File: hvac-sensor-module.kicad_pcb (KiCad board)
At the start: 2 copper layers, 30 x 41 mm, 53 parts, among them J1 Conn_01x04, P1 Debug, Q1 RSS060P05FRATB, SW1 SW_PUSH, SW2 SW_PUSH, SW3 SW_PUSH, U1 LMR16006, U2 HDC1080, U3 STM32F072C8Tx, U5 TCAN334, X1 32.768KHz 12.5pF

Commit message: Layout finished.
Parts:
- removed C10, C12: 15p, Capacitor_SMD:C_0603_1608Metric_Pad1.05x0.95mm_HandSolder
- removed C2: 0.1F, villa-control:CP_Radial_D13.0mm_P10mm
- removed D3: 0.3V, villa-control:D_SOD-123_HandSolder
- removed R3: 100, Resistors_SMD:R_0603_HandSoldering
- removed the REF** at (124.0, 92.0)
- removed W2: 3.3V, TestPoint:TestPoint_THTPad_D1.5mm_Drill0.7mm
- removed W3: GND, TestPoint:TestPoint_THTPad_1.5x1.5mm_Drill0.7mm
- removed X1: 32.768KHz 12.5pF, villa-control:Crystal-MS1V-T1K
- added C18: 4µ7, Capacitor_SMD:C_0805_2012Metric_Pad1.15x1.40mm_HandSolder, F.Cu at (147.5, 112.5)
- added J2: Sensor, villa-control:Solder_Connecor_1x04, F.Cu at (145.0, 114.5)
- added J3: Sensor, villa-control:Solder_Connecor_1x04, F.Cu at (145.0, 118.5)
- added REF**: Break_Drills_Sensor, villa-control:Break_Drills_Sensor, F.Cu at (145.0, 116.2)
- added REF**: OSHW-Logo2_7.3x6mm_SilkScreen, Symbol:OSHW-Logo2_7.3x6mm_SilkScreen, B.Cu at (158.5, 121.5)
- added REF**: Drill_2mm, villa-control:Drill_2mm, F.Cu at (156.0, 117.0)
- added REF**: Drill_2mm, villa-control:Drill_2mm, F.Cu at (134.0, 117.0)
- added REF**: Drill_2mm, villa-control:Drill_2mm, F.Cu at (145.0, 94.0)
- added REF**: Drill_1mm, villa-control:Drill_1mm, F.Cu at (141.5, 123.5)
- added REF**: Drill_1mm, villa-control:Drill_1mm, F.Cu at (148.5, 123.5)
- added TP1: PA7, TestPoint:TestPoint_Pad_1.0x1.0mm, F.Cu at (141.2, 114.5)
- added TP11: NRST, TestPoint:TestPoint_Pad_1.5x1.5mm, B.Cu at (145.0, 104.8)
- added TP14: CAN_TX, TestPoint:TestPoint_Pad_1.5x1.5mm, B.Cu at (130.5, 103.2)
- added TP15: CAN_RX, TestPoint:TestPoint_Pad_1.5x1.5mm, B.Cu at (130.5, 106.8)
- added TP18: VINC, TestPoint:TestPoint_Pad_1.0x1.0mm, B.Cu at (154.0, 82.0)
- added TP19: 3.3V, TestPoint:TestPoint_THTPad_D1.5mm_Drill0.7mm, F.Cu at (162.5, 105.2)
- added TP2: PA6, TestPoint:TestPoint_Pad_1.0x1.0mm, F.Cu at (139.2, 114.5)
- added TP20: GND, TestPoint:TestPoint_THTPad_1.5x1.5mm_Drill0.7mm, F.Cu at (162.5, 108.5)
- added TP21: BOOT0, TestPoint:TestPoint_Pad_1.0x1.0mm, B.Cu at (146.0, 96.5)
- added TP3: PA5, TestPoint:TestPoint_Pad_1.0x1.0mm, F.Cu at (137.2, 114.5)
- added TP4: PA4, TestPoint:TestPoint_Pad_1.0x1.0mm, F.Cu at (135.2, 114.5)
- added TP5: USART2_RX, TestPoint:TestPoint_Pad_1.0x1.0mm, F.Cu at (133.2, 114.5)
- added TP6: USART2_TX, TestPoint:TestPoint_Pad_1.0x1.0mm, B.Cu at (136.2, 106.5)
- J1, P1: moved to B.Cu
- moved C9 77.4 mm to (154.8, 121.8)
- moved C5 68.4 mm to (148.5, 121.0), turned to 270 degrees
- moved R9 68.2 mm to (160.0, 116.5)
- moved D2 67.9 mm to (149.5, 85.0), turned to 270 degrees
- moved D5 67.5 mm to (160.0, 115.0), turned to 180 degrees
- moved R7 66.1 mm to (154.8, 120.2)
- moved D4 65.8 mm to (155.0, 88.0), turned to 180 degrees
- moved C15 64.3 mm to (152.8, 102.2), turned to 270 degrees
- moved R2 63.8 mm to (157.5, 82.0), turned to 180 degrees
- moved R8 63.2 mm to (152.0, 111.8), turned to 270 degrees
- moved C4 61.7 mm to (154.0, 94.0), turned to 90 degrees
- moved R6 61.0 mm to (153.5, 111.8), turned to 270 degrees
- moved L1 59.8 mm to (160.0, 94.0), turned to 270 degrees
- moved U1 59.7 mm to (160.0, 85.5), turned to 90 degrees
- moved C3 58.3 mm to (163.5, 87.5), turned to 90 degrees
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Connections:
- net Net-(C1-Pad1) renamed /power supply/VIN_DCDC
- net Net-(R6-Pad2) renamed /microcontroller/SCL
- net Net-(R8-Pad2) renamed /microcontroller/SDA
- U3 pad 1: +BATT -> +3.3VADC
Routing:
- net GND: track 0.00 -> 164.2 mm, vias 0 -> 33
- net +3.3VADC: track 0.00 -> 143.9 mm, vias 0 -> 9
- net Net-(D6-Pad2): track 0.00 -> 46.6 mm, vias 0 -> 2
- net Net-(C6-Pad1): track 0.00 -> 41.8 mm, vias 0 -> 2
- net /microcontroller/NRST: track 0.00 -> 30.6 mm, vias 0 -> 2
- net /microcontroller/SCL: track 0.00 -> 29.6 mm, vias 0 -> 2
- net /microcontroller/SDA: track 0.00 -> 26.6 mm, vias 0 -> 2
- net Net-(TP14-Pad1): track 0.00 -> 26.5 mm, vias 0 -> 2
- net Net-(C9-Pad1): track 0.00 -> 25.4 mm
- net Net-(TP15-Pad1): track 0.00 -> 24.6 mm, vias 0 -> 2
- net Net-(U3-Pad10): track 0.00 -> 20.4 mm
- net CANL_IN: track 0.00 -> 19.8 mm
- net CANH_IN: track 0.00 -> 18.0 mm
- net Net-(D5-Pad2): track 0.00 -> 17.3 mm
- net Net-(U3-Pad11): track 0.00 -> 16.2 mm
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- added copper zone on F.Cu, net +3.3VADC
- added copper zone on F.Cu, net +VIN
- added copper zone on F.Cu, net /power supply/VIN_DCDC
- added copper zone on B.Cu, net GND
- added copper zone on F.Cu, net GND
- added copper zone on F.Cu, net Net-(C3-Pad1)
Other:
- board size 30 x 41 mm -> 40 x 45 mm
- net class 0,5mm added: clearance 0.2, trace_width 0.5, via_dia 0.8, via_drill 0.4
- rule pad_to_mask_clearance: 0.051 -> 0
- rule trace_min: 0.2 -> 0.1
- board text added: "VillaControl HVAC Sensor Module 1.0"

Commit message: Update D1.
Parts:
- added TP10: USB_D+, TestPoint:TestPoint_Pad_1.5x1.5mm, F.Cu at (155.8, 71.8)
- added TP9: USB_D-, TestPoint:TestPoint_Pad_1.5x1.5mm, F.Cu at (153.3, 71.8)
- D1: footprint Diodes_SMD:D_SMA_Handsoldering -> Diode_SMD:D_SMB_Handsoldering
- moved D1 0.71 mm to (140.0, 85.5)

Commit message: Change test point.
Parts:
- removed TP18: VINC, TestPoint:TestPoint_Pad_1.0x1.0mm
- removed TP21: BOOT0, TestPoint:TestPoint_Pad_1.0x1.0mm
- removed the TP9 at (153.3, 71.8)
- added TP12: CAN_TX, villa-control:TestPoint_Pad_D0.75mm, B.Cu at (130.5, 103.2)
- added TP13: CAN_RX, villa-control:TestPoint_Pad_D0.75mm, B.Cu at (130.5, 106.8)
- added TP7: VINC, villa-control:TestPoint_Pad_D0.75mm, B.Cu at (154.0, 82.0)
- TP1, TP2, TP3, TP4, TP5, TP6: footprint TestPoint:TestPoint_Pad_1.0x1.0mm -> villa-control:TestPoint_Pad_D0.75mm
- TP10: value USB_D+ -> NRST; footprint TestPoint:TestPoint_Pad_1.5x1.5mm -> villa-control:TestPoint_Pad_D0.75mm; moved to B.Cu
- TP11: value NRST -> BOOT0; footprint TestPoint:TestPoint_Pad_1.5x1.5mm -> villa-control:TestPoint_Pad_D0.75mm
- TP14: value CAN_TX -> USB_D-; footprint TestPoint:TestPoint_Pad_1.5x1.5mm -> villa-control:TestPoint_Pad_D0.75mm
- TP15: value CAN_RX -> USB_D+; footprint TestPoint:TestPoint_Pad_1.5x1.5mm -> villa-control:TestPoint_Pad_D0.75mm
- moved TP10 34.7 mm to (145.0, 104.8), turned to 180 degrees
- moved TP15 12.0 mm to (130.0, 94.8)
- moved TP11 9.22 mm to (147.0, 95.8)
- moved TP14 7.02 mm to (130.0, 96.2)
- moved TP5 2.00 mm to (135.2, 114.5), turned to 0 degrees
- moved TP4 1.50 mm to (136.8, 114.5), turned to 0 degrees
- moved TP3 1.00 mm to (138.2, 114.5), turned to 0 degrees
- moved TP2 0.50 mm to (139.8, 114.5), turned to 0 degrees
- renumbered TP19 to TP8, TP20 to TP9
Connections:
- TP10 pad 1: Net-(TP10-Pad1) -> /microcontroller/NRST
- TP11 pad 1: /microcontroller/NRST -> Net-(TP11-Pad1)
- U3 pad 32: Net-(TP9-Pad1) -> Net-(TP14-Pad1)
- U3 pad 33: Net-(TP10-Pad1) -> Net-(TP15-Pad1)
- U3 pad 44: Net-(TP21-Pad1) -> Net-(TP11-Pad1)
- U3 pad 45: Net-(TP15-Pad1) -> Net-(TP13-Pad1)
- U3 pad 46: Net-(TP14-Pad1) -> Net-(TP12-Pad1)
- U5 pad 1: Net-(TP14-Pad1) -> Net-(TP12-Pad1)
- U5 pad 4: Net-(TP15-Pad1) -> Net-(TP13-Pad1)
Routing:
- net Net-(TP12-Pad1): track 0.00 -> 26.5 mm, vias 0 -> 2
- net Net-(TP13-Pad1): track 0.00 -> 24.6 mm, vias 0 -> 2
- net Net-(TP21-Pad1): track 6.89 -> 0.00 mm, vias 1 -> 0
- net Net-(TP11-Pad1): track 0.00 -> 6.08 mm, vias 0 -> 1
- net Net-(TP4-Pad1): track 10.7 -> 8.83 mm
- net Net-(TP5-Pad1): track 11.6 -> 9.75 mm
- net Net-(TP15-Pad1): track 24.6 -> 26.0 mm, vias 2 -> 1
- net Net-(TP3-Pad1): track 9.26 -> 7.91 mm
- net GND: track 164.2 -> 165.4 mm, vias 33 -> 35
- net Net-(TP14-Pad1): track 26.5 -> 26.4 mm, vias 2 -> 1
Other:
- board text added: "C"
- board text added: "D"
- board text added: "G"
- board text added: "Rev. 1.0"
- board text added: "V"

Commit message: Clean up references.
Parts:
- removed REF**: Break_Drills_Sensor, villa-control:Break_Drills_Sensor
- removed REF**: OSHW-Logo2_7.3x6mm_SilkScreen, Symbol:OSHW-Logo2_7.3x6mm_SilkScreen
- removed REF** (x3): Drill_2mm, villa-control:Drill_2mm
- removed REF** (x2): Drill_1mm, villa-control:Drill_1mm
- renumbered C14 to C10, C13 to C12, C21 to C13, C7 to C14, C18 to C16, C3 to C2, C4 to C3, C16 to C4, C19 to C7, D4 to D3, D7 to D4, R12 to R10, R13 to R11, R5 to R3, R6 to R4, R8 to R5, R4 to R6, R9 to R8, R10 to R9

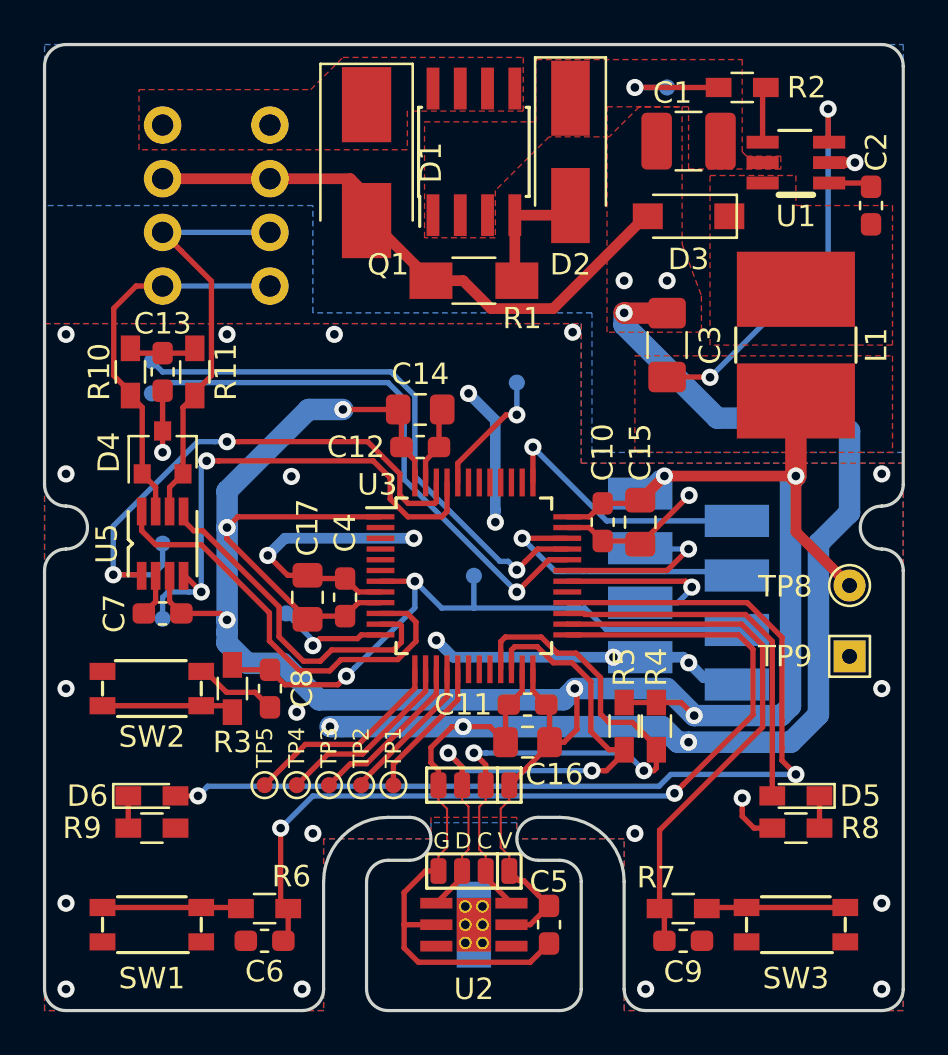
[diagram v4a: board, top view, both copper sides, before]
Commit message: Update some footprints and fine tuning.
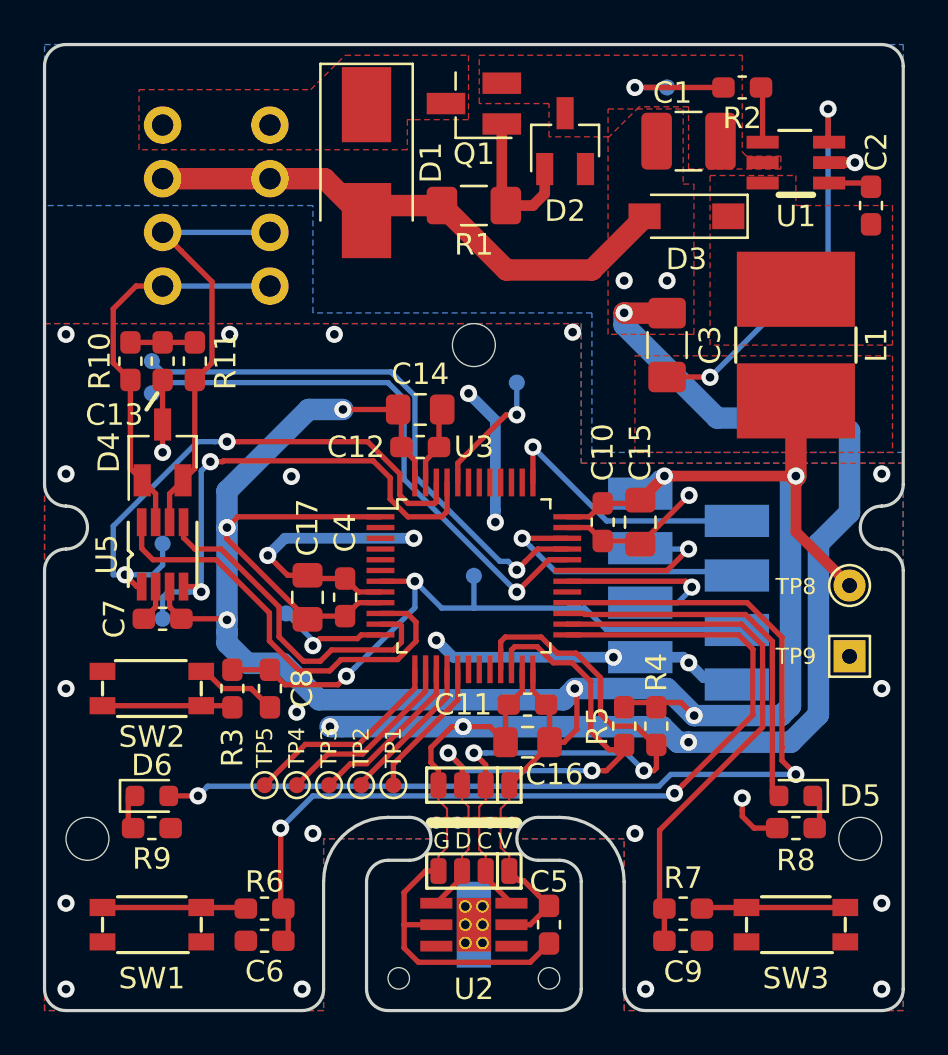
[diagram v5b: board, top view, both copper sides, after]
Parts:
- added REF**: Drill_1mm, villa-control:Drill_1mm, F.Cu at (148.5, 123.5)
- added REF**: Drill_2mm, villa-control:Drill_2mm, F.Cu at (145.0, 94.0)
- added REF**: Drill_2mm, villa-control:Drill_2mm, F.Cu at (163.0, 117.0)
- added REF**: Drill_2mm, villa-control:Drill_2mm, F.Cu at (127.0, 117.0)
- added REF**: Drill_1mm, villa-control:Drill_1mm, F.Cu at (141.5, 123.5)
- added REF**: Break_Drills_Sensor, villa-control:Break_Drills_Sensor, F.Cu at (145.0, 116.2)
- added REF**: OSHW-Logo2_7.3x6mm_SilkScreen, Symbol:OSHW-Logo2_7.3x6mm_SilkScreen, B.Cu at (161.0, 95.5)
- D2: footprint Diodes_SMD:D_SMA_Handsoldering -> villa-control:D_SOT-23_ANK_Handsolder
- D3: footprint villa-control:D_SOD-123_HandSolder -> villa-control:D_SOD-123_Handsolder
- D4: footprint TO_SOT_Packages_SMD:SOT-23 -> villa-control:SOT-23_Handsoldering
- D5, D6: footprint LEDs:LED_0603_HandSoldering -> LED_SMD:LED_0603_1608Metric_Pad0.88x0.95mm_HandSolder
- Q1: value RSS060P05FRATB -> FDN5618P; footprint villa-control:SOIC-8_3.9x4.9mm_Pitch1.27mm_11123333 -> villa-control:SuperSOT-3_HandSoldering
- R1: footprint Resistors_SMD:R_1206_HandSoldering -> Resistor_SMD:R_1206_3216Metric_Pad1.42x1.75mm_HandSolder
- R10, R11, R2, R3, R4, R5, R6, R7, R8, R9: footprint Resistors_SMD:R_0603_HandSoldering -> Resistor_SMD:R_0603_1608Metric_Pad1.05x0.95mm_HandSolder
- U3: footprint Housings_QFP:LQFP-48_7x7mm_Pitch0.5mm -> Package_QFP:LQFP-48_7x7mm_P0.5mm
- moved R1 3.50 mm to (145.0, 87.5)
- moved Q1 2.25 mm to (145.0, 82.8), turned to 180 degrees
- moved D2 0.56 mm to (149.2, 84.5), turned to 90 degrees
- moved C13 0.50 mm to (130.5, 94.8)
- moved R10 0.50 mm to (129.0, 94.8)
- moved R11 0.50 mm to (132.0, 94.8)
- moved U5 0.50 mm to (130.5, 103.8)
- moved C7 0.25 mm to (130.5, 106.8)
- moved D3 0.10 mm to (154.9, 88.0)
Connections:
- Q1 pad 1: /power supply/VIN_DCDC -> Net-(D2-Pad2)
- Q1 pad 2: Net-(D2-Pad2) -> /power supply/VIN_DCDC
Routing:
- net GND: track 165.4 -> 164.1 mm
- net Net-(D2-Pad2): track 5.87 -> 7.07 mm
- net CANH_IN: track 18.0 -> 18.5 mm
- net CANL_IN: track 19.8 -> 20.3 mm

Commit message: some cleanup
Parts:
- removed the REF** at (145.0, 94.0)
- removed the REF** at (163.0, 117.0)
- removed the REF** at (127.0, 117.0)
- removed the REF** at (145.0, 116.2)
- removed the REF** at (161.0, 95.5)
- added REF**: Drill_2mm, villa-control:Drill_2mm, F.Cu at (163.0, 113.0)
- added REF**: Drill_2mm, villa-control:Drill_2mm, F.Cu at (127.0, 113.0)
- added REF**: Drill_2mm, villa-control:Drill_2mm, F.Cu at (127.0, 82.0)
- added REF**: Drill_2mm, villa-control:Drill_2mm, F.Cu at (163.0, 82.0)
- C17: value 1µ -> 4µ7
- C2: value 100n >10V -> 100n
- C4: value 10n -> 100n
- D3: value 50V Vr 1A -> 50V Vrrm 1A
- L1: footprint villa-control:SDE0604A_HandSoldering -> villa-control:L_Bourns-SDR0604
- R1: footprint Resistor_SMD:R_1206_3216Metric_Pad1.42x1.75mm_HandSolder -> Resistor_SMD:R_0603_1608Metric_Pad1.05x0.95mm_HandSolder
- moved D3 0.50 mm to (154.9, 88.5)
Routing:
- net GND: track 164.1 -> 162.4 mm, vias 35 -> 36

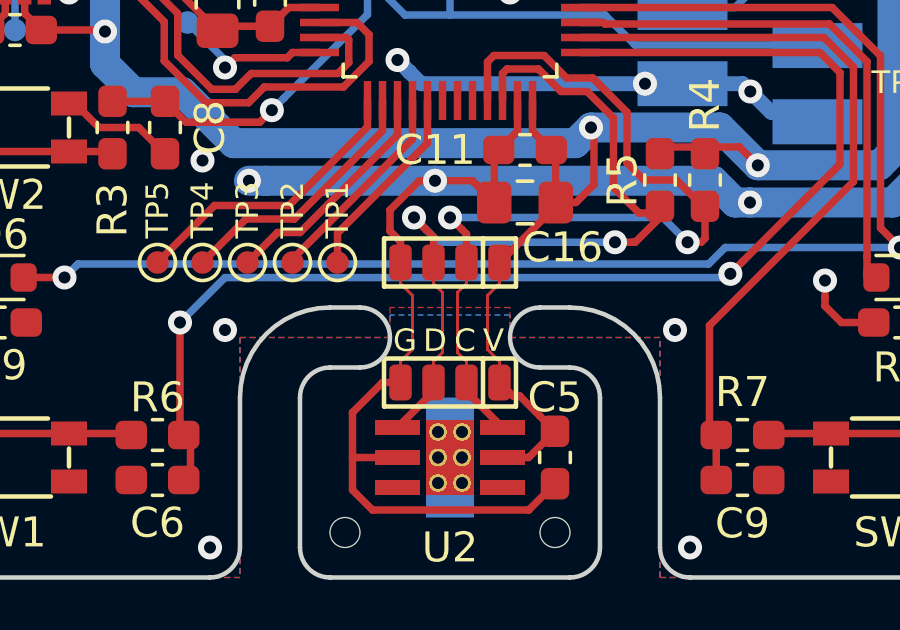
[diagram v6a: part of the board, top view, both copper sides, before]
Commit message: Add some logos to PCB and update panel.
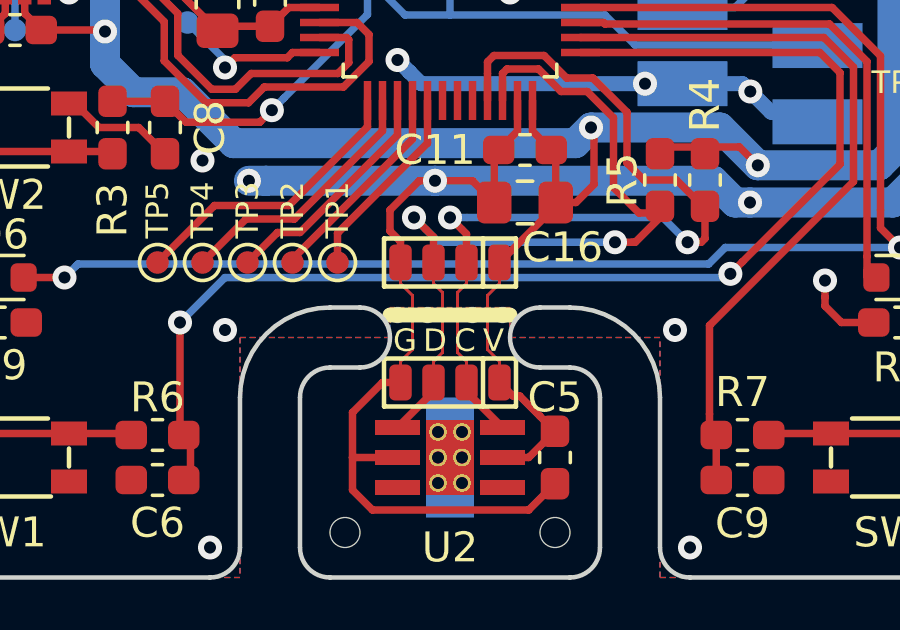
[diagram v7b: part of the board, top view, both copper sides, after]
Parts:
- added REF**: KiCad-Logo2_6mm_SilkScreen, Symbol:KiCad-Logo2_6mm_SilkScreen, B.Cu at (131.7, 116.0)
- added REF**: Break_Drills_Sensor, villa-control:Break_Drills_Sensor, F.Cu at (145.0, 116.2)
- added REF**: OSHW-Logo2_7.3x6mm_SilkScreen, Symbol:OSHW-Logo2_7.3x6mm_SilkScreen, B.Cu at (158.4, 120.0)
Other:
- board text added: "VillaControl HVAC Sensor Module"
- board text removed: "VillaControl HVAC Sensor Module 1.0"
